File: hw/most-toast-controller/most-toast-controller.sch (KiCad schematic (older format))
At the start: 3 parts

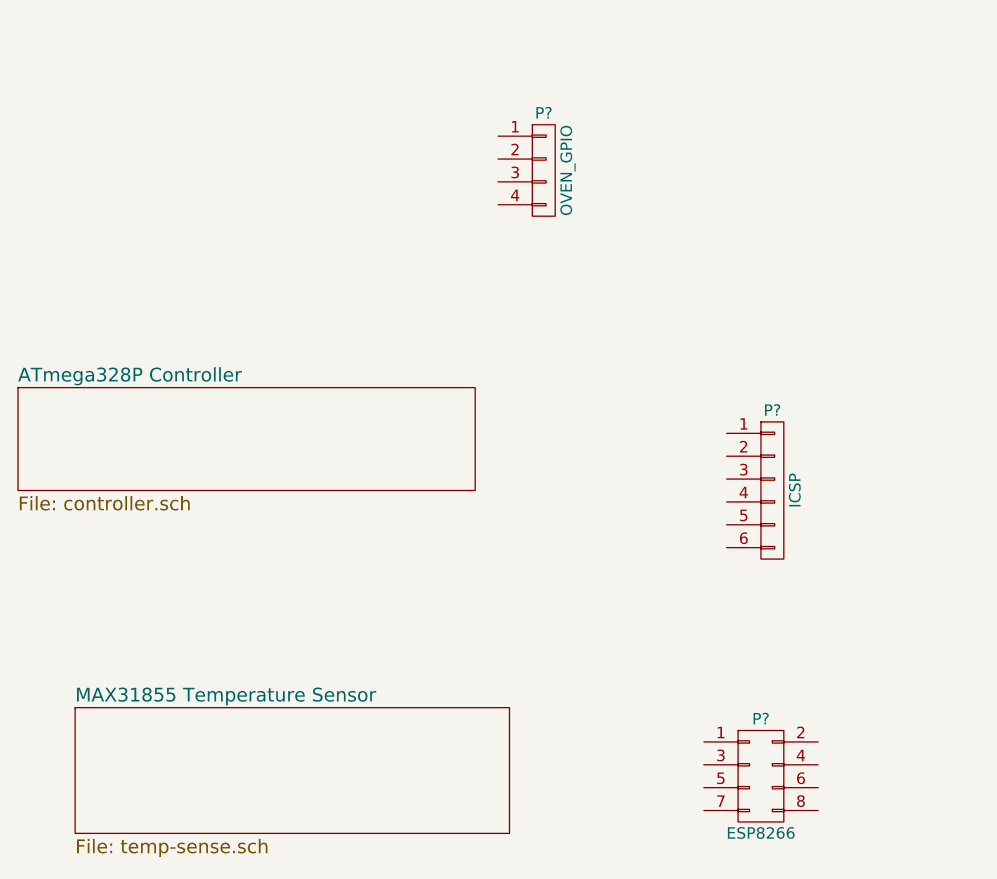
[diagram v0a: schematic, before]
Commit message: most-toast schematic finished.
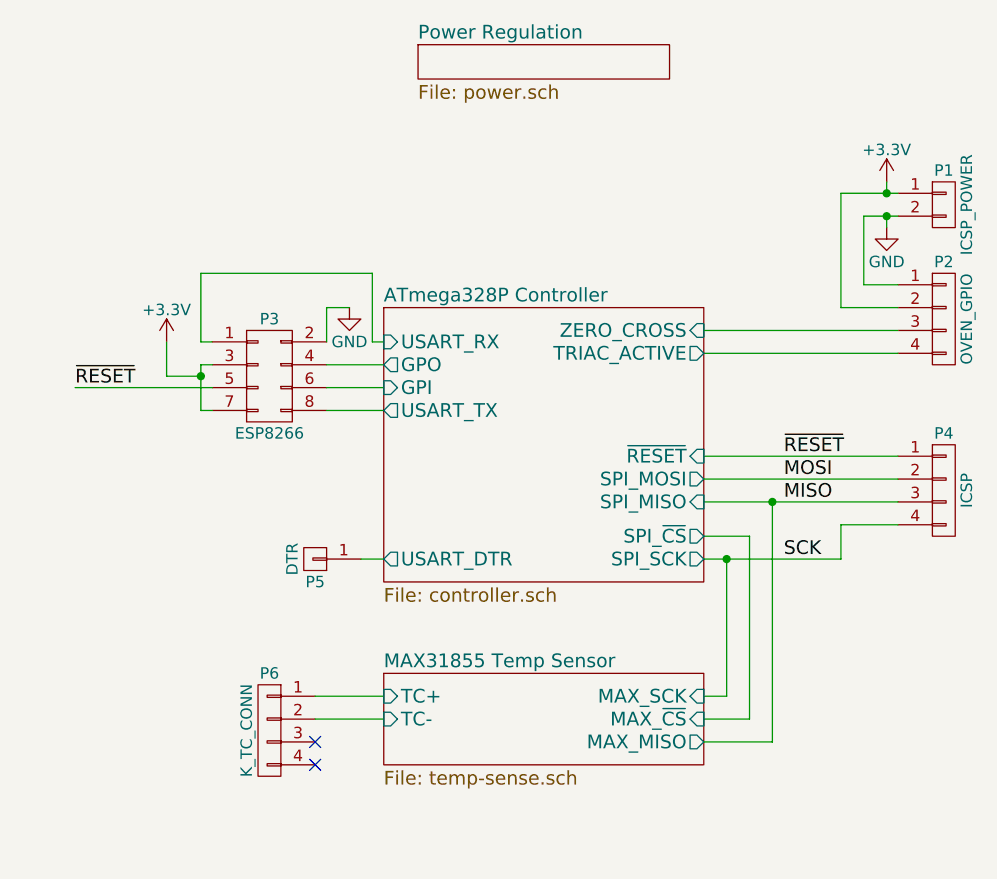
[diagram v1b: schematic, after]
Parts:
- removed P?: ICSP, symbol CONN_01X06
- added P1: ICSP_POWER, symbol CONN_01X02
- added P4: ICSP, symbol CONN_01X04
- added P5: DTR, symbol CONN_01X01
- added P6: K_TC_CONN, symbol CONN_01X04
- gave numbers to parts that had none: 2
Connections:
- net ATmega328P Controller/USART_RX: now reaches P3.1 (P1)
- net GND: now reaches P3.2 (P2)
- net GND: now also P2.1 (P1), P1.2 (P2)
- net +3V3: now reaches P3.3 (P3)
- net +3V3: now also P2.2 (P2), P3.7 (P7), P1.1 (P1)
- net ATmega328P Controller/GPO: now reaches P3.4 (P4)
- net ~RESET: now reaches P3.5 (P5)
- net ~RESET: now also P4.1 (P1)
- net ATmega328P Controller/GPI: now reaches P3.6 (P6)
- net ATmega328P Controller/USART_TX: now reaches P3.8 (P8)
- net ATmega328P Controller/ZERO_CROSS: now reaches P2.3 (P3)
- net ATmega328P Controller/TRIAC_ACTIVE: now reaches P2.4 (P4)
- new net ATmega328P Controller/USART_DTR: P5.1 (P1)
- new net MAX31855 Temp Sensor/TC+: P6.1 (P1)
- new net MAX31855 Temp Sensor/TC-: P6.2 (P2)
- new net MISO: P4.3 (P3)
- new net MOSI: P4.2 (P2)
- new net SCK: P4.4 (P4)
- no-connect marks 0 -> 2
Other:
- moved on the sheet: P2, P3

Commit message: started putting most-toast on a board. Turns out one inch makes for very very small PCB
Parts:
- removed P6: K_TC_CONN, symbol CONN_01X04
- added P6: TC_CONN, tc-conns:OSTTE020104, symbol CONN_01X02
- P1: footprint (none) -> Pin_Headers:Pin_Header_Straight_1x02
- P2, P4: footprint (none) -> Pin_Headers:Pin_Header_Straight_1x04
- P3: footprint (none) -> Pin_Headers:Pin_Header_Straight_2x04
- P5: footprint (none) -> Pin_Headers:Pin_Header_Straight_1x01
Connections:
- net MAX31855 Temp Sensor/TC+: now also P6.2 (P2)
- net MAX31855 Temp Sensor/TC-: now also P6.1 (P1)
- no-connect marks 2 -> 0
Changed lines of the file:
@@
 EESchema Schematic File Version 2
+LIBS:regul
 LIBS:power
 LIBS:device
@@
 LIBS:conn
 LIBS:linear
-LIBS:regul
 LIBS:74xx
 LIBS:cmos4000
@@
 F 0 "P3" H 5100 2850 50  0000 C CNN
 F 1 "ESP8266" H 5100 2350 50  0000 C CNN
-F 2 "" H 5100 1400 60  0000 C CNN
+F 2 "Pin_Headers:Pin_Header_Straight_2x04" H 5100 1400 60  0001 C CNN
 F 3 "" H 5100 1400 60  0000 C CNN
 	1    5100 2600
@@
 F 0 "P2" H 8050 2600 50  0000 C CNN
 F 1 "OVEN_GPIO" V 8150 2350 50  0000 C CNN
-F 2 "" H 8050 2350 60  0000 C CNN
+F 2 "Pin_Headers:Pin_Header_Straight_1x04" H 8050 2350 60  0001 C CNN
 F 3 "" H 8050 2350 60  0000 C CNN
 	1    8050 2350
@@
 $EndComp
 $Comp
-L +3.3V #PWR1
+L +3.3V #PWR01
 U 1 1 564A9669
 P 7800 1750
-F 0 "#PWR1" H 7800 1600 50  0001 C CNN
+F 0 "#PWR01" H 7800 1600 50  0001 C CNN
 F 1 "+3.3V" H 7800 1890 50  0000 C CNN
 F 2 "" H 7800 1750 60  0000 C CNN
@@
 $EndComp
 $Comp
-L GND #PWR2
+L GND #PWR02
 U 1 1 564A9717
 P 7800 1950
-F 0 "#PWR2" H 7800 1700 50  0001 C CNN
+F 0 "#PWR02" H 7800 1700 50  0001 C CNN
 F 1 "GND" H 7800 1800 50  0000 C CNN
 F 2 "" H 7800 1950 60  0000 C CNN
@@
 $EndComp
 $Comp
-L GND #PWR3
+L GND #PWR03
 U 1 1 564B8375
 P 5450 2300
-F 0 "#PWR3" H 5450 2050 50  0001 C CNN
+F 0 "#PWR03" H 5450 2050 50  0001 C CNN
 F 1 "GND" H 5450 2150 50  0000 C CNN
 F 2 "" H 5450 2300 60  0000 C CNN
@@
 $EndComp
 $Comp
-L +3.3V #PWR4
+L +3.3V #PWR04
 U 1 1 564B9F70
 P 4650 2450
-F 0 "#PWR4" H 4650 2300 50  0001 C CNN
+F 0 "#PWR04" H 4650 2300 50  0001 C CNN
 F 1 "+3.3V" H 4650 2590 50  0000 C CNN
 F 2 "" H 4650 2450 60  0000 C CNN
@@
 $EndSheet
 $Comp
-L CONN_01X04 P6
-U 1 1 564BC68D
-P 5100 4150
-F 0 "P6" H 5100 4400 50  0000 C CNN
-F 1 "K_TC_CONN" V 5200 4150 50  0000 C CNN
-F 2 "" H 5100 4150 60  0000 C CNN
-F 3 "" H 5100 4150 60  0000 C CNN
-	1    5100 4150
-	-1   0    0    -1
-$EndComp
-NoConn ~ 5300 4300
-NoConn ~ 5300 4200
-$Comp
 L CONN_01X01 P5
 U 1 1 564C66D5
@@
 F 0 "P5" H 5300 3500 50  0000 C CNN
 F 1 "DTR" V 5400 3400 50  0000 C CNN
-F 2 "" H 5300 3400 60  0000 C CNN
+F 2 "Pin_Headers:Pin_Header_Straight_1x01" H 5300 3400 60  0001 C CNN
 F 3 "" H 5300 3400 60  0000 C CNN
 	1    5300 3400
@@
 F 0 "P4" H 8050 3350 50  0000 C CNN
 F 1 "ICSP" V 8150 3100 50  0000 C CNN
-F 2 "" H 8050 3100 60  0000 C CNN
+F 2 "Pin_Headers:Pin_Header_Straight_1x04" H 8050 3100 60  0001 C CNN
 F 3 "" H 8050 3100 60  0000 C CNN
 	1    8050 3100
@@
 F 0 "P1" H 8050 2000 50  0000 C CNN
 F 1 "ICSP_POWER" V 8150 1850 50  0000 C CNN
-F 2 "" H 8050 1850 60  0000 C CNN
+F 2 "Pin_Headers:Pin_Header_Straight_1x02" H 8050 1850 60  0001 C CNN
 F 3 "" H 8050 1850 60  0000 C CNN
 	1    8050 1850
@@
 	4650 2450 4650 2600
 Wire Wire Line
-	5300 4000 5600 4000
-Wire Wire Line
-	5300 4100 5600 4100
+	5500 4000 5600 4000
+Wire Wire Line
+	5500 4100 5600 4100
 Wire Wire Line
 	7000 3300 7200 3300
@@
 	7600 2300 7600 1800
 $Sheet
-S 5750 1150 1100 150
+S 5700 1700 1100 150
 U 564DC657
 F0 "Power Regulation" 60
@@
 Wire Wire Line
 	5600 3400 5500 3400
+$Comp
+L CONN_01X02 P6
+U 1 1 5653B1E8
+P 5300 4050
+F 0 "P6" H 5300 4200 50  0000 C CNN
+F 1 "TC_CONN" V 5400 4050 50  0000 C CNN
+F 2 "tc-conns:OSTTE020104" H 5300 4050 60  0001 C CNN
+F 3 "" H 5300 4050 60  0000 C CNN
+	1    5300 4050
+	-1   0    0    1
+$EndComp
 $EndSCHEMATC
